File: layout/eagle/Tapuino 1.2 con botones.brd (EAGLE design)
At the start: 100 x 47 mm, 12 parts, among them CN1 C64_CASETTE_EDGE, IC1 4052N, IC2 ARDUINO_NANO_V3

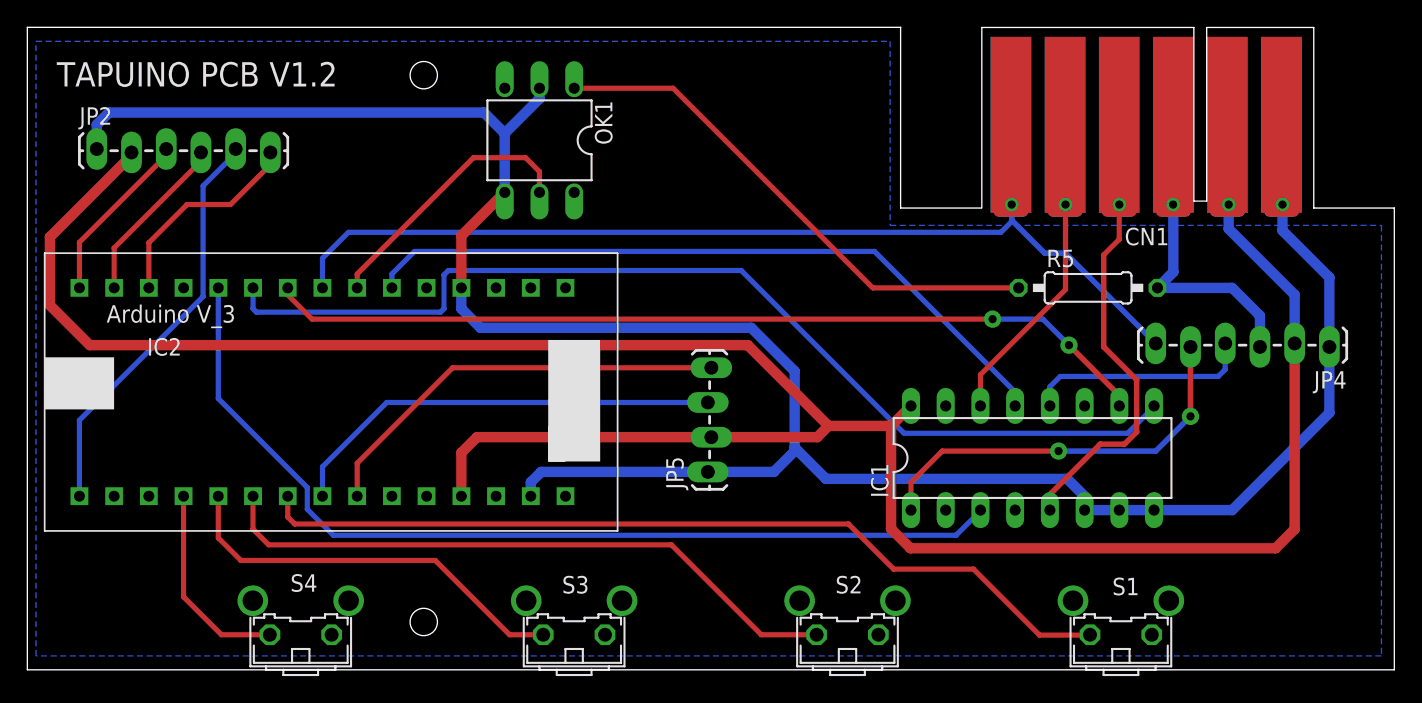
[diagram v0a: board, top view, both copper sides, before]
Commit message: Added spcbm 1.2 board, removed mine
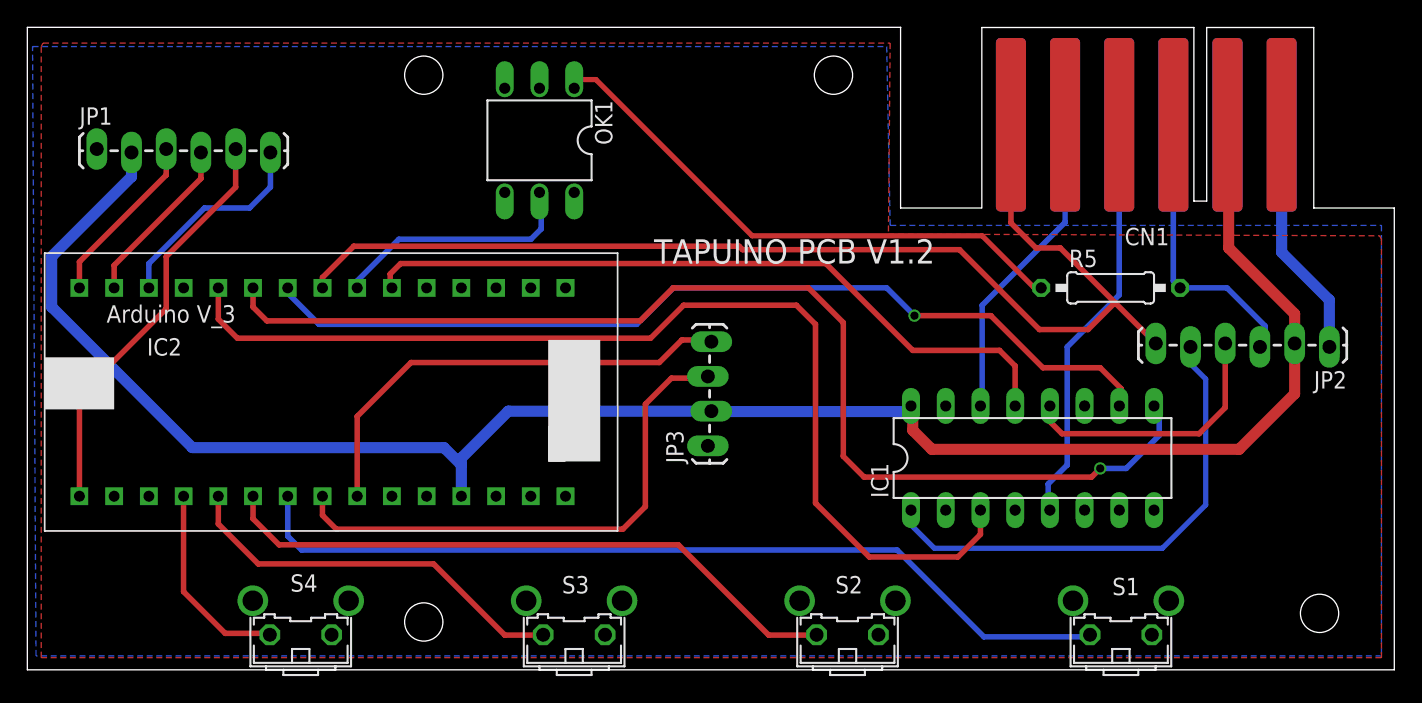
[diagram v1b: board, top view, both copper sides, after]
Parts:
- removed JP4: C64 CON, SparkFun:1X06_LOCK_LONGPADS
- removed JP5: LCD_SHIELD, SparkFun:1X04_LOCK_LONGPADS
- added JP1: SD_SHIELD, SparkFun:1X06_LOCK_LONGPADS
- added JP3: LCD_SHIELD, SparkFun:1X04_LOCK_LONGPADS
- CN1: device commodore:C64_CASSETTE -> commodore MOD:C64_CASSETTE
- JP2: value SD_SHIELD -> C64 CON
- moved JP2 91.3 mm to (95.2, 23.6), turned to 180 degrees
- moved R5 1.65 mm to (79.2, 27.9)
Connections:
- net GND: now also JP1.1, JP3.1; no longer JP4.1, JP5.1
- net N$1: now also JP1.3; no longer JP2.3
- net N$13: now also JP2.5; no longer JP4.5
- net N$14: now also JP2.3; no longer JP4.3
- net N$16: now also JP2.4; no longer JP4.4
- net N$17: now also JP2.6; no longer JP4.6
- net N$2: now also JP1.6; no longer JP2.6
- net N$3: now also JP1.5; no longer JP2.5
- net N$4: now also JP1.4; no longer JP2.4
- net N$5: now also JP3.4; no longer JP5.4
- net N$6: now also JP3.3; no longer JP5.3
- net VCC: now also JP1.2, JP3.2; no longer JP4.2, JP5.2
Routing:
- net GND: track 167.7 -> 18.2 mm, vias 1 -> 0
- net VCC: track 178.7 -> 139.7 mm, vias 1 -> 0
- net N$17: track 70.7 -> 84.4 mm, vias 1 -> 0
- net N$20: track 76.0 -> 84.2 mm, vias 0 -> 1
- net N$15: track 69.7 -> 77.4 mm
- net N$13: track 29.6 -> 36.7 mm, vias 2 -> 0
- net N$6: track 32.3 -> 39.0 mm
- net N$21: track 19.0 -> 23.1 mm, vias 1 -> 0
- net N$16: track 16.7 -> 19.8 mm
- net N$5: track 31.2 -> 34.1 mm
- net N$22: track 65.1 -> 67.8 mm, vias 2 -> 1
- net N$14: track 18.9 -> 21.2 mm, vias 1 -> 0
- net N$8: track 38.6 -> 40.8 mm
- net N$10: track 19.8 -> 18.3 mm
- net N$19: track 29.1 -> 30.4 mm, vias 1 -> 0
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- added copper zone on layer 1, net GND
